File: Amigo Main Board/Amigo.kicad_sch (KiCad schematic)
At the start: 39 parts, among them J1 USB_C_Receptacle_USB2.0_16P, J2 Conn_01x02, J3 SH1106 OLED, J4 MAX98357A, J5 DRV8833, J6 ButtonRibbonConnector, SW1 SW_Push, SW2 SW_Push, U1 TP4056-42-ESOP8, U2 AP2112K-3.3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

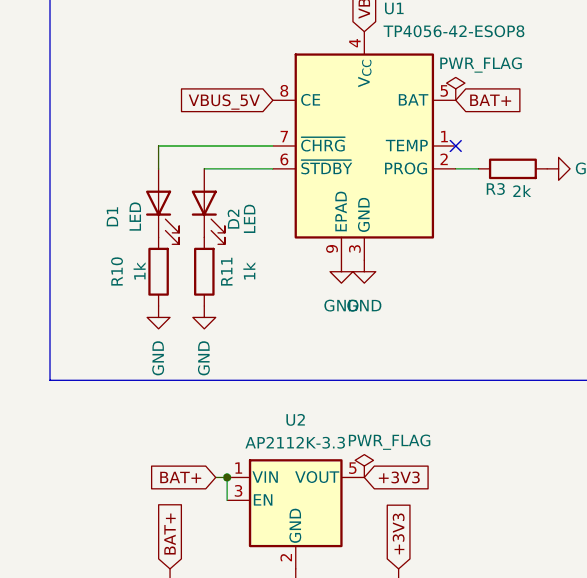
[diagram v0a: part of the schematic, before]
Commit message: fixed LED polarity
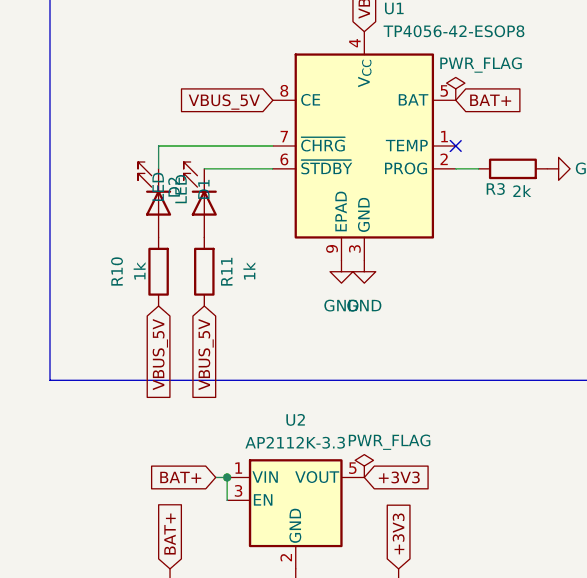
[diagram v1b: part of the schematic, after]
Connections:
- net GND: no longer R10.1, R11.1
- net VBUS_5V: now also R10.1, R11.1
- net at D1.1 (K): now also U1.7 (~{CHRG}); no longer R10.2
- net at D1.2 (A): now also R10.2; no longer U1.7 (~{CHRG})
- net at R11.2: now also D2.2 (A); no longer D2.1 (K)
- net at U1.6 (~{STDBY}): now also D2.1 (K); no longer D2.2 (A)
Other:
- moved on the sheet: D1, D2
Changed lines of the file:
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@@
 		)
 	)
+	(global_label "VBUS_5V"
+		(shape input)
+		(at 34.29 114.3 270)
+		(fields_autoplaced yes)
+		(effects
+			(font
+				(size 1.27 1.27)
+			)
+			(justify right)
+		)
+		(property "Intersheetrefs" "${INTERSHEET_REFS}"
+			(at 34.29 124.5234 90)
+			(hide yes)
+			(show_name no)
+			(do_not_autoplace no)
+			(effects
+				(font
+					(size 1.27 1.27)
+				)
+				(justify right)
+			)
+		)
+	)
 	(global_label "BUTTON_COL_1"
 		(shape input)
@@
 		)
 	)
+	(global_label "VBUS_5V"
+		(shape input)
+		(at 29.21 114.3 270)
+		(fields_autoplaced yes)
+		(effects
+			(font
+				(size 1.27 1.27)
+			)
+			(justify right)
+		)
+		(property "Intersheetrefs" "${INTERSHEET_REFS}"
+			(at 29.21 124.5234 90)
+			(hide yes)
+			(show_name no)
+			(do_not_autoplace no)
+			(effects
+				(font
+					(size 1.27 1.27)
+				)
+				(justify right)
+			)
+		)
+	)
 	(global_label "USB_CC1"
 		(shape input)
@@
 	)
 	(symbol
-		(lib_id "power:GND")
-		(at 34.29 114.3 0)
-		(unit 1)
-		(body_style 1)
-		(exclude_from_sim no)
-		(in_bom yes)
-		(on_board yes)
-		(in_pos_files yes)
-		(dnp no)
-		(fields_autoplaced yes)
-		(property "Reference" "#PWR022"
-			(at 34.29 120.65 0)
-			(hide yes)
-			(show_name no)
-			(do_not_autoplace no)
-			(effects
-				(font
-					(size 1.27 1.27)
-				)
-			)
-		)
-		(property "Value" "GND"
-			(at 34.29 118.11 90)
-			(show_name no)
-			(do_not_autoplace no)
-			(effects
-				(font
-					(size 1.27 1.27)
-				)
-				(justify right)
-			)
-		)
-		(property "Footprint" ""
-			(at 34.29 114.3 0)
-			(hide yes)
-			(show_name no)
-			(do_not_autoplace no)
-			(effects
-				(font
-					(size 1.27 1.27)
-				)
-			)
-		)
-		(property "Datasheet" ""
-			(at 34.29 114.3 0)
-			(hide yes)
-			(show_name no)
-			(do_not_autoplace no)
-			(effects
-				(font
-					(size 1.27 1.27)
-				)
-			)
-		)
-		(property "Description" "Power symbol creates a global label with name \"GND\" , ground"
-			(at 34.29 114.3 0)
-			(hide yes)
-			(show_name no)
-			(do_not_autoplace no)
-			(effects
-				(font
-					(size 1.27 1.27)
-				)
-			)
-		)
-		(pin "1"
-		)
-		(instances
-			(project "Amigo"
-				(path "/f7f379f1-5a8a-4021-8619-544cc3f6930e"
-					(reference "#PWR022")
-					(unit 1)
-				)
-			)
-		)
-	)
-	(symbol
 		(lib_id "Device:LED")
-		(at 29.21 102.87 90)
+		(at 29.21 102.87 270)
 		(unit 1)
 		(body_style 1)
@@
 		(dnp no)
 		(property "Reference" "D1"
-			(at 24.13 104.394 0)
+			(at 34.29 101.346 0)
 			(show_name no)
 			(do_not_autoplace no)
@@
 		)
 		(property "Value" "LED"
-			(at 26.67 104.394 0)
+			(at 31.75 101.346 0)
 			(show_name no)
 			(do_not_autoplace no)
@@
 	(symbol
 		(lib_id "Device:LED")
-		(at 34.29 102.87 90)
+		(at 34.29 102.87 270)
 		(unit 1)
 		(body_style 1)
@@
 		(dnp no)
 		(property "Reference" "D2"
-			(at 37.592 104.648 0)
+			(at 30.988 101.092 0)
 			(show_name no)
 			(do_not_autoplace no)
@@
 		)
 		(property "Value" "LED"
-			(at 39.37 104.648 0)
+			(at 29.21 101.092 0)
 			(show_name no)
 			(do_not_autoplace no)
@@
 					(unit 1)
 				)
-			)
-		)
-	)
-	(symbol
-		(lib_id "power:GND")
-		(at 29.21 114.3 0)
-		(unit 1)
-		(body_style 1)
-		(exclude_from_sim no)
-		(in_bom yes)
-		(on_board yes)
-		(in_pos_files yes)
-		(dnp no)
-		(fields_autoplaced yes)
-		(property "Reference" "#PWR021"
-			(at 29.21 120.65 0)
-			(hide yes)
-			(show_name no)
-			(do_not_autoplace no)
-			(effects
-				(font
-					(size 1.27 1.27)
-				)
-			)
-		)
-		(property "Value" "GND"
-			(at 29.21 118.11 90)
-			(show_name no)
-			(do_not_autoplace no)
-			(effects
-				(font
-					(size 1.27 1.27)
-				)
-				(justify right)
-			)
-		)
-		(property "Footprint" ""
-			(at 29.21 114.3 0)
-			(hide yes)
-			(show_name no)
-			(do_not_autoplace no)
-			(effects
-				(font
-					(size 1.27 1.27)
-				)
-			)
-		)
-		(property "Datasheet" ""
-			(at 29.21 114.3 0)
-			(hide yes)
-			(show_name no)
-			(do_not_autoplace no)
-			(effects
-				(font
-					(size 1.27 1.27)
-				)
-			)
-		)
-		(property "Description" "Power symbol creates a global label with name \"GND\" , ground"
-			(at 29.21 114.3 0)
-			(hide yes)
-			(show_name no)
-			(do_not_autoplace no)
-			(effects
-				(font
-					(size 1.27 1.27)
-				)
-			)
-		)
-		(pin "1"
-		)
-		(instances
-			(project "Amigo"
-				(path "/f7f379f1-5a8a-4021-8619-544cc3f6930e"
-					(reference "#PWR021")
-					(unit 1)
-				)

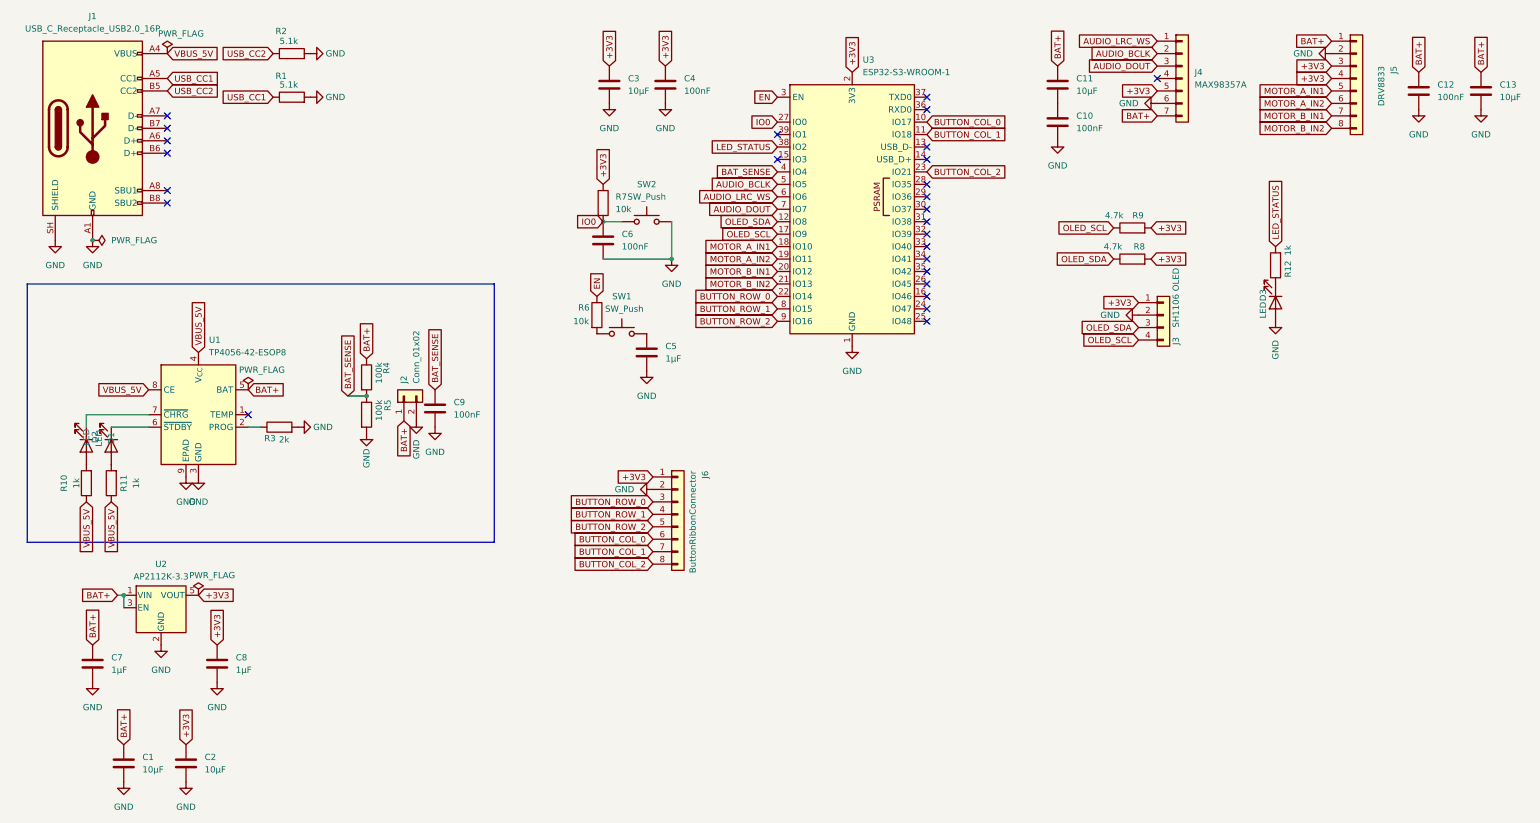
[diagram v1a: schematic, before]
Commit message: Finished wiring up the new OLED
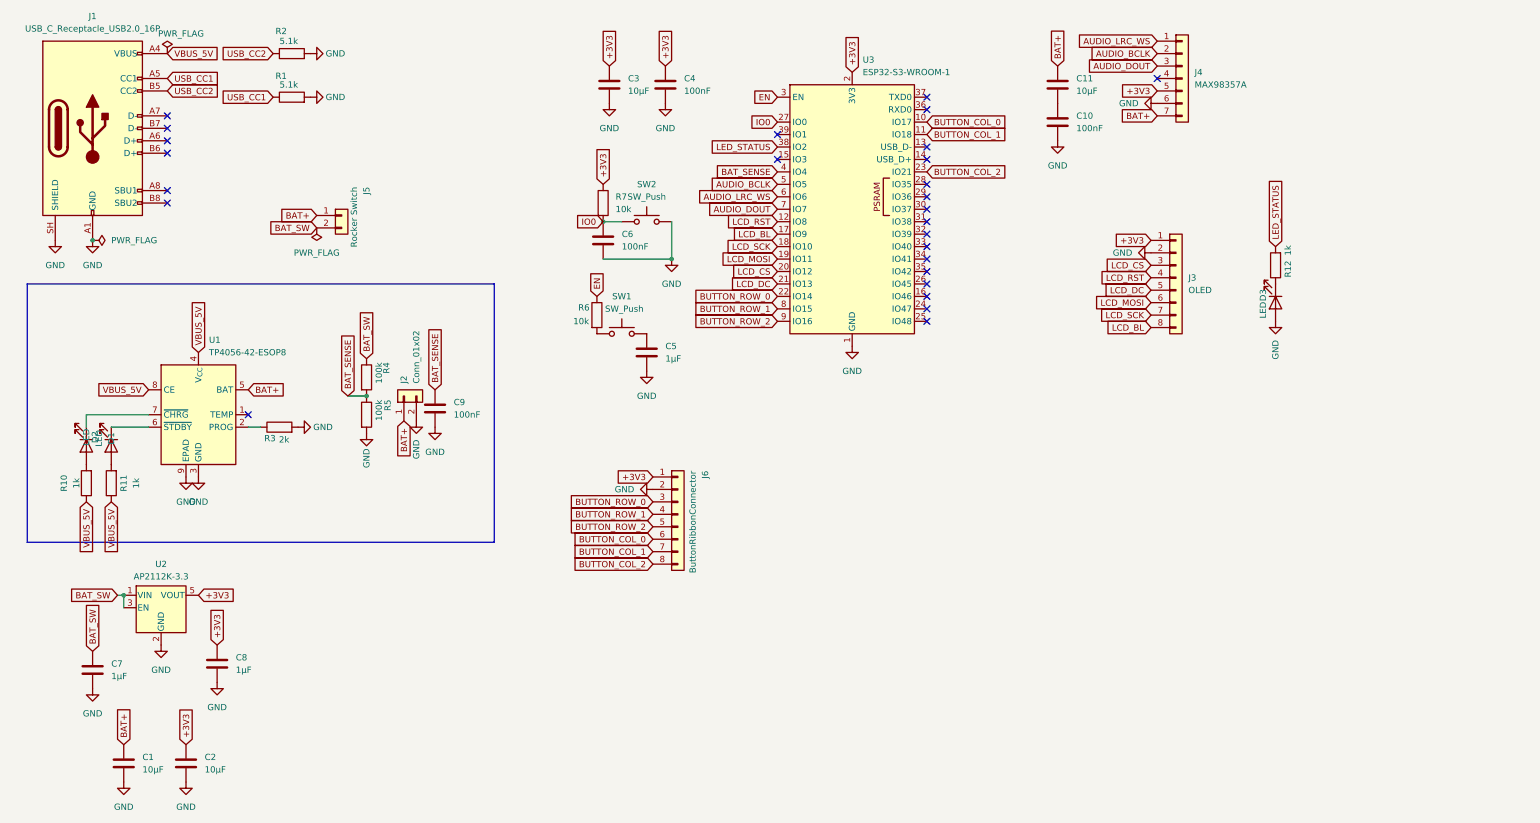
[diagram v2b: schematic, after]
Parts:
- removed C12: 100nF, Capacitor_SMD:C_0603_1608Metric, symbol Device:C
- removed C13: 10µF, Capacitor_SMD:C_0805_2012Metric, symbol Device:C
- removed J3: SH1106 OLED, Connector_PinHeader_2.54mm:PinHeader_1x04_P2.54mm_Vertical, symbol Connector_Generic:Conn_01x04
- removed J5: DRV8833, Connector_PinHeader_2.54mm:PinHeader_1x08_P2.54mm_Vertical, symbol Connector_Generic:Conn_01x08
- removed R8, R9: 4.7k, Resistor_SMD:R_0603_1608Metric, symbol Device:R
- added J3: OLED, Connector_PinHeader_2.54mm:PinHeader_1x08_P2.54mm_Vertical, symbol Connector_Generic:Conn_01x08
- added J5: Rocker Switch, Connector_PinHeader_2.54mm:PinHeader_1x02_P2.54mm_Vertical, symbol Connector_Generic:Conn_01x02
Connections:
- net +3V3: now also J3.1 (Pin_1)
- net BAT+: now also J5.1 (Pin_1); no longer C7.1, R4.1, U2.1 (VIN), U2.3 (EN)
- net GND: now also J3.2 (Pin_2)
- net MOTOR_A_IN1 renamed LCD_SCK
- net LCD_SCK: now also J3.7 (Pin_7)
- net MOTOR_A_IN2 renamed LCD_MOSI
- net LCD_MOSI: now also J3.6 (Pin_6)
- net MOTOR_B_IN1 renamed LCD_CS
- net LCD_CS: now also J3.3 (Pin_3)
- net MOTOR_B_IN2 renamed LCD_DC
- net LCD_DC: now also J3.5 (Pin_5)
- net OLED_SCL renamed LCD_BL
- net LCD_BL: now also J3.8 (Pin_8)
- net OLED_SDA renamed LCD_RST
- net LCD_RST: now also J3.4 (Pin_4)
- new net BAT_SW: C7.1, J5.2 (Pin_2), R4.1, U2.1 (VIN), U2.3 (EN)
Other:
- moved on the sheet: C7

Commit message: gerber and stuff
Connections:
- net +3V3: now also R6.1; no longer J4.5 (Pin_5)
- net BAT+: now also C10.1
- net EN: now also C5.1, R6.2, SW1.1; no longer R6.1
- net GND: now also C11.2, SW1.2
- no-connect marks 26 -> 27
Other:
- moved on the sheet: C10, C11, C5, J4, R6, SW1
